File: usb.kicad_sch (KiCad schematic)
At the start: 4 parts, among them J1001 USB_B

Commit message: completed schematic
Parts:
- added C701: 100nF, Capacitor_SMD:C_0603_1608Metric, symbol Device:C
- added U1001: USBLC6-2P6, Package_TO_SOT_SMD:SOT-666, symbol Power_Protection:USBLC6-2P6
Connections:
- net GND: now also C701.2, U1001.2 (GND)
- net at FB1001.2, J1001.1 (VBUS): now also C701.1, U1001.5 (VBUS)
- net at J1001.2 (D-): now also U1001.1 (I/O1); no longer R1002.2
- net at J1001.3 (D+): now also U1001.3 (I/O2); no longer R1001.2
- new net: R1001.2, U1001.4 (I/O2)
- new net: R1002.2, U1001.6 (I/O1)
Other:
- note removed: "ToDo: ESD Prot. fehlt Footprint Stecker checken!!"
- moved on the sheet: FB1001, J1001, R1001, R1002

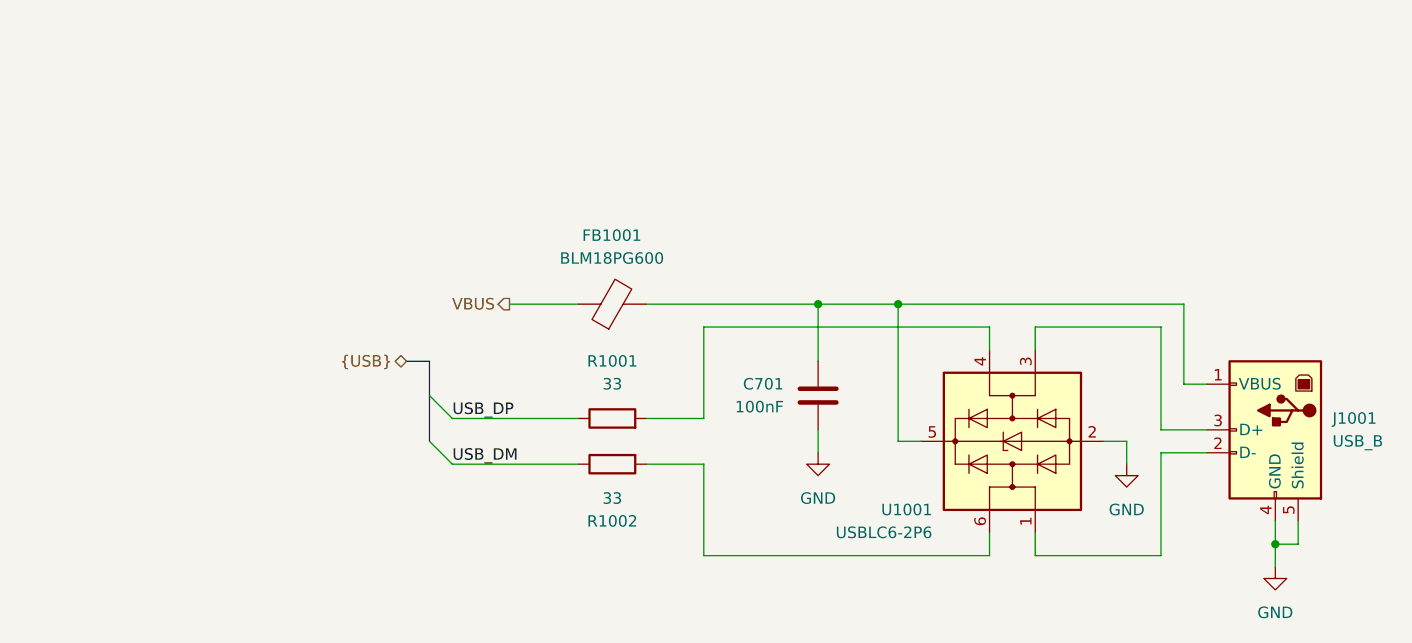
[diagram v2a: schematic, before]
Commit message: hierarchical sheets for digital I/O and replaced power supply jumpers with relays
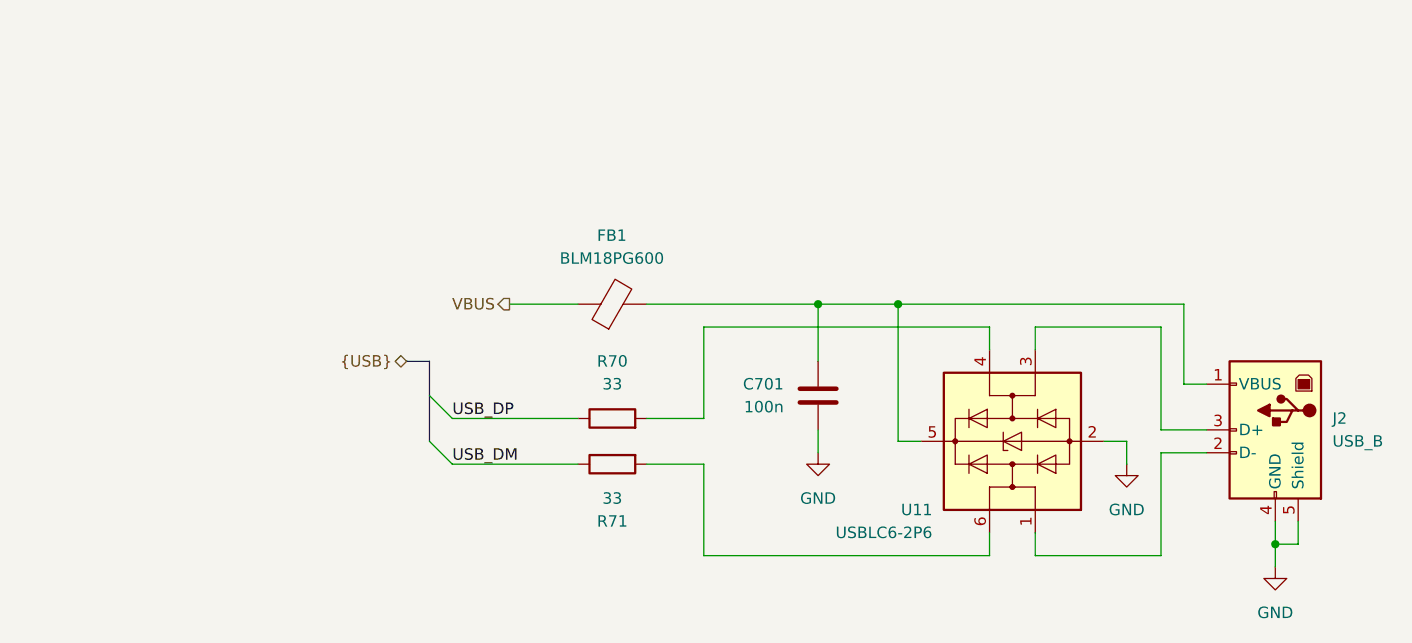
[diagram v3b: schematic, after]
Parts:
- C701: value 100nF -> 100n
- renumbered FB1001 to FB1, J1001 to J2, R1001 to R70, R1002 to R71, U1001 to U11
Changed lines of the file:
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@@
   (symbol (lib_id "Power_Protection:USBLC6-2P6") (at 135.89 66.04 90) (unit 1)
     (in_bom yes) (on_board yes) (dnp no)
-    (property "Reference" "U1001" (at 127 73.66 90)
+    (property "Reference" "U11" (at 127 73.66 90)
       (effects (font (size 1.27 1.27)) (justify left))
     )
@@
       (project "Sensor_Board"
         (path "/e2a0eb17-0eae-4cdd-befd-118f8728b921/8460c5f0-f567-411d-b3a7-76d8207879f4"
-          (reference "U1001") (unit 1)
+          (reference "U11") (unit 1)
         )
       )
@@
   (symbol (lib_id "Device:FerriteBead") (at 91.44 50.8 90) (unit 1)
     (in_bom yes) (on_board yes) (dnp no) (fields_autoplaced)
-    (property "Reference" "FB1001" (at 91.3892 43.18 90)
+    (property "Reference" "FB1" (at 91.3892 43.18 90)
       (effects (font (size 1.27 1.27)))
     )
@@
       (project "Sensor_Board"
         (path "/e2a0eb17-0eae-4cdd-befd-118f8728b921/8460c5f0-f567-411d-b3a7-76d8207879f4"
-          (reference "FB1001") (unit 1)
-        )
-      )
-      (project "FT22_VCU_Konzept"
-        (path "/e63e39d7-6ac0-4ffd-8aa3-1841a4541b55/3c48a9d0-891a-4016-826f-62373ede344c"
           (reference "FB1") (unit 1)
         )
       )
+      (project "FT22_VCU_Konzept"
+        (path "/e63e39d7-6ac0-4ffd-8aa3-1841a4541b55/3c48a9d0-891a-4016-826f-62373ede344c"
+          (reference "FB1") (unit 1)
+        )
+      )
     )
   )
   (symbol (lib_id "Connector:USB_B") (at 165.1 64.77 0) (mirror y) (unit 1)
     (in_bom yes) (on_board yes) (dnp no) (fields_autoplaced)
-    (property "Reference" "J1001" (at 171.45 63.4999 0)
+    (property "Reference" "J2" (at 171.45 63.4999 0)
       (effects (font (size 1.27 1.27)) (justify right))
     )
@@
       (project "Sensor_Board"
         (path "/e2a0eb17-0eae-4cdd-befd-118f8728b921/8460c5f0-f567-411d-b3a7-76d8207879f4"
-          (reference "J1001") (unit 1)
+          (reference "J2") (unit 1)
         )
       )
@@
   (symbol (lib_id "power:GND") (at 165.1 80.01 0) (unit 1)
     (in_bom yes) (on_board yes) (dnp no) (fields_autoplaced)
-    (property "Reference" "#PWR01001" (at 165.1 86.36 0)
+    (property "Reference" "#PWR0144" (at 165.1 86.36 0)
       (effects (font (size 1.27 1.27)) hide)
     )
@@
       (project "Sensor_Board"
         (path "/e2a0eb17-0eae-4cdd-befd-118f8728b921/8460c5f0-f567-411d-b3a7-76d8207879f4"
-          (reference "#PWR01001") (unit 1)
+          (reference "#PWR0144") (unit 1)
         )
       )
@@
   (symbol (lib_id "Device:R") (at 91.44 63.5 90) (unit 1)
     (in_bom yes) (on_board yes) (dnp no) (fields_autoplaced)
-    (property "Reference" "R1001" (at 91.44 57.15 90)
+    (property "Reference" "R70" (at 91.44 57.15 90)
       (effects (font (size 1.27 1.27)))
     )
@@
       (project "Sensor_Board"
         (path "/e2a0eb17-0eae-4cdd-befd-118f8728b921/8460c5f0-f567-411d-b3a7-76d8207879f4"
-          (reference "R1001") (unit 1)
+          (reference "R70") (unit 1)
         )
       )
@@
   (symbol (lib_id "power:GND") (at 114.3 67.31 0) (unit 1)
     (in_bom yes) (on_board yes) (dnp no) (fields_autoplaced)
-    (property "Reference" "#PWR01003" (at 114.3 73.66 0)
+    (property "Reference" "#PWR0142" (at 114.3 73.66 0)
       (effects (font (size 1.27 1.27)) hide)
     )
@@
       (project "Sensor_Board"
         (path "/e2a0eb17-0eae-4cdd-befd-118f8728b921/8460c5f0-f567-411d-b3a7-76d8207879f4"
-          (reference "#PWR01003") (unit 1)
+          (reference "#PWR0142") (unit 1)
         )
       )
@@
       (effects (font (size 1.27 1.27)) (justify left))
     )
-    (property "Value" "100nF" (at 110.49 62.2299 0)
+    (property "Value" "100n" (at 110.49 62.2299 0)
       (effects (font (size 1.27 1.27)) (justify left))
     )
@@
         )
         (path "/e2a0eb17-0eae-4cdd-befd-118f8728b921/8460c5f0-f567-411d-b3a7-76d8207879f4"
-          (reference "C1001") (unit 1)
+          (reference "C60") (unit 1)
         )
       )
@@
   (symbol (lib_id "Device:R") (at 91.44 68.58 90) (mirror x) (unit 1)
     (in_bom yes) (on_board yes) (dnp no)
-    (property "Reference" "R1002" (at 91.44 74.93 90)
+    (property "Reference" "R71" (at 91.44 74.93 90)
       (effects (font (size 1.27 1.27)))
     )
@@
       (project "Sensor_Board"
         (path "/e2a0eb17-0eae-4cdd-befd-118f8728b921/8460c5f0-f567-411d-b3a7-76d8207879f4"
-          (reference "R1002") (unit 1)
+          (reference "R71") (unit 1)
         )
       )
@@
   (symbol (lib_id "power:GND") (at 148.59 68.58 0) (unit 1)
     (in_bom yes) (on_board yes) (dnp no) (fields_autoplaced)
-    (property "Reference" "#PWR01002" (at 148.59 74.93 0)
+    (property "Reference" "#PWR0143" (at 148.59 74.93 0)
       (effects (font (size 1.27 1.27)) hide)
     )
@@
       (project "Sensor_Board"
         (path "/e2a0eb17-0eae-4cdd-befd-118f8728b921/8460c5f0-f567-411d-b3a7-76d8207879f4"
-          (reference "#PWR01002") (unit 1)
-        )
-      )
+          (reference "#PWR0143") (unit 1)
+        )
+      )
